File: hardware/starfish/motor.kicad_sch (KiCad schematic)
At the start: 24 parts, among them J7 MOTOR, U8 TMC2209

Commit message: First pass at schematic for starfish
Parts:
- added C1411: 100u, Capacitor_SMD:CP_Elec_6.3x9.9, symbol Device:C_Polarized_Small_US
- R1402: renamed from R18; value 220m -> 120m
- R1403: renamed from R19; value 220m -> 120m
- renumbered C28 to C1401, C29 to C1402, C30 to C1403, C31 to C1404, C32 to C1405, C33 to C1406, C38 to C1407, C39 to C1408, C40 to C1409, C41 to C1410, C35 to C1412, C36 to C1413, C37 to C1414, FB2 to FB1401, FB3 to FB1402, FB4 to FB1403, FB5 to FB1404, J7 to J1401, R17 to R1401, RV2 to RV1401, RV3 to RV1402, U8 to U1401
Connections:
- net GND: now also C1411.2
- net VS renamed +24V
- net +24V: now also C1411.1
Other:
- note added: "* Keep close to TMC2209 pin 28 (VS)"
- note added: "* Keep close to header"
- note added: "* Maximum current limited to 1.64 A(RMS) with R(sense) R18, R19 at 220mΩ * ESD & EME circuitry per Datasheet 3.7 * Bypass capacitors per Datasheet 3.1 * Internal clock set by CLK pulled low * SPREAD left floating since configuration is done via UART"
- note removed: "* Maximum current limited to 1 A(RMS) with R(sense) R18, R19 at 220mΩ * ESD & EME circuitry per Datasheet 3.7 * Bypass capacitors per Datasheet 3.1 * Internal clock set by CLK pulled low * SPREAD left floating since configuration is done via UART"
- title: Jellyfish -> Starfish
- moved on the sheet: C1401, C1402, C1403, C1404, C1405, C1406, C1407, C1408, C1409, C1410, C1412, C1413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

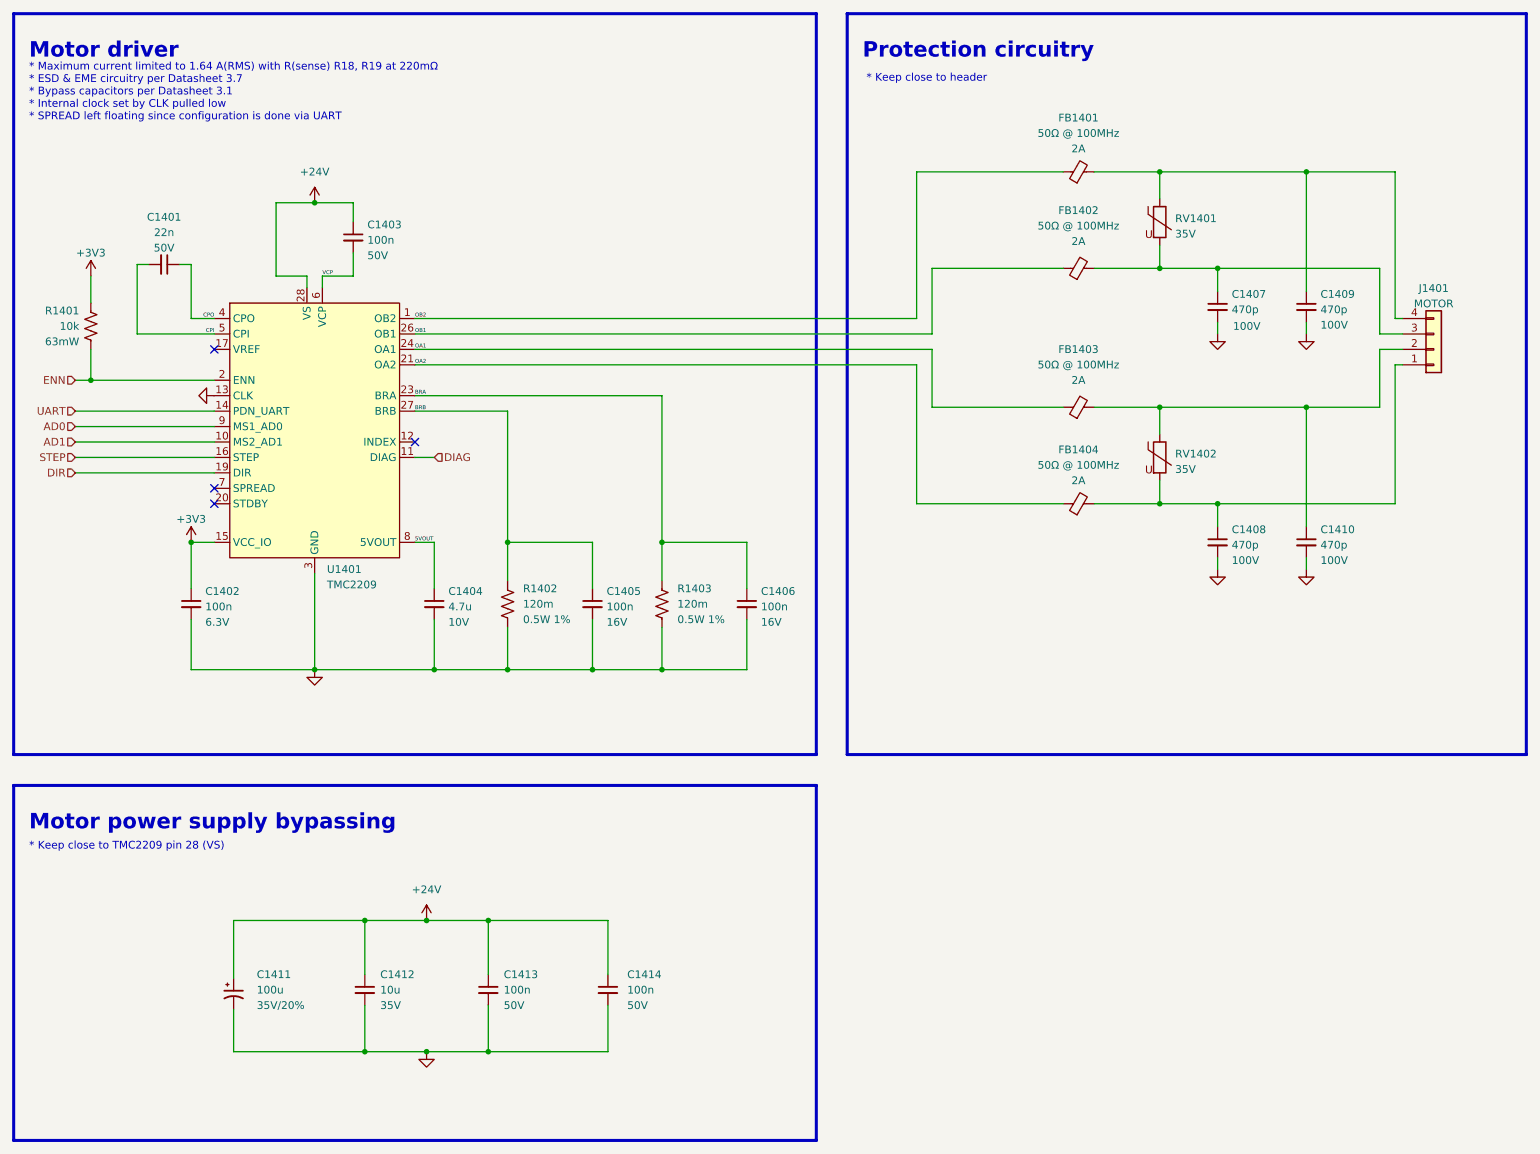
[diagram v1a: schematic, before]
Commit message: Mostly finished starfish schematic, ready for layout!
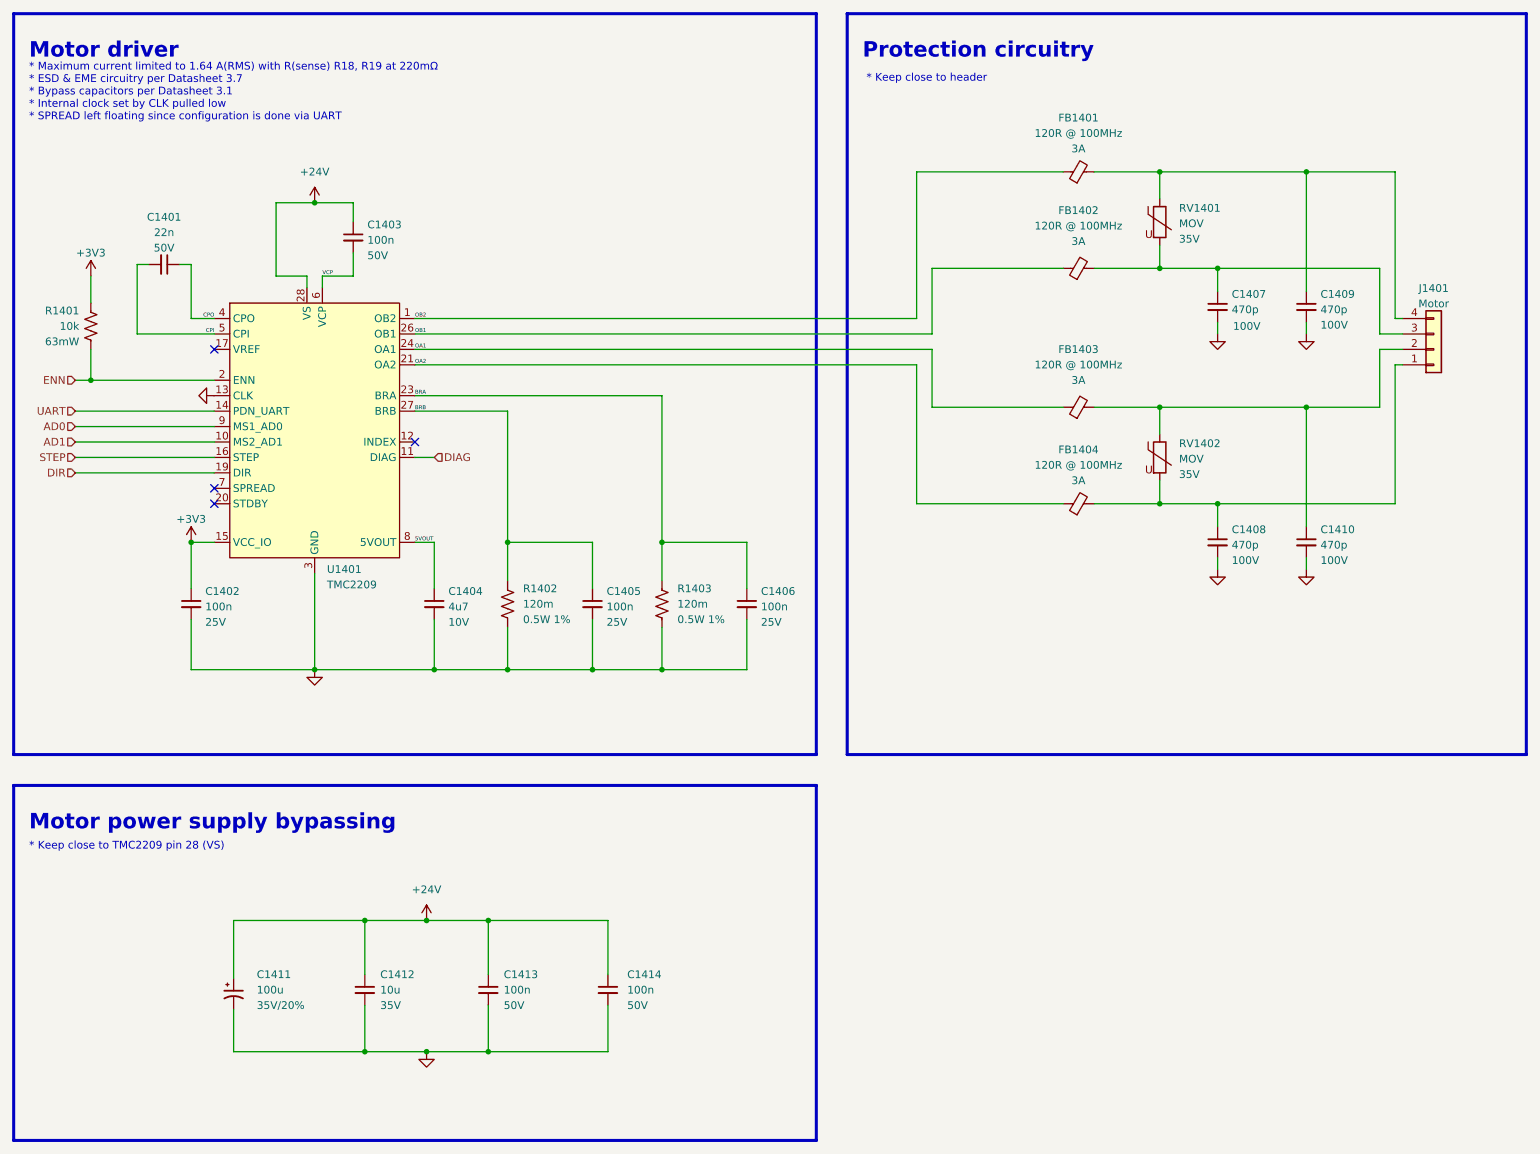
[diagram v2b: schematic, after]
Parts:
- C1401, C1403, C1407, C1408, C1409, C1410, C1413, C1414: footprint Capacitor_SMD:C_0603_1608Metric_Pad1.08x0.95mm_HandSolder -> winterbloom:C_0603_HandSolder
- C1402: footprint Capacitor_SMD:C_0402_1005Metric_Pad0.74x0.62mm_HandSolder -> winterbloom:C_0402_HandSolder; Rating 6.3V -> 25V
- C1404: value 4.7u -> 4u7; footprint Capacitor_SMD:C_0603_1608Metric_Pad1.08x0.95mm_HandSolder -> winterbloom:C_0603_HandSolder
- C1405, C1406: footprint Capacitor_SMD:C_0402_1005Metric_Pad0.74x0.62mm_HandSolder -> winterbloom:C_0402_HandSolder; Rating 16V -> 25V
- C1412: footprint Capacitor_SMD:C_1210_3225Metric_Pad1.33x2.70mm_HandSolder -> winterbloom:C_1210_HandSolder
- FB1401, FB1402, FB1403, FB1404: value 50Ω @ 100MHz -> 120R @ 100MHz; Rating 2A -> 3A
- J1401: value MOTOR -> Motor
- R1401: footprint Resistor_SMD:R_0402_1005Metric_Pad0.72x0.64mm_HandSolder -> winterbloom:R_0402_HandSolder
- RV1401, RV1402: value 35V -> MOV; Rating (none) -> 35V

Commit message: Layout and routing mostly done! Just gotta make it prettier!
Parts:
- FB1401, FB1402, FB1403, FB1404: footprint Inductor_SMD:L_0603_1608Metric_Pad1.05x0.95mm_HandSolder -> winterbloom:L_0603_HandSolder
- J1401: footprint Connector_JST:JST_XH_B4B-XH-AM_1x04_P2.50mm_Vertical -> winterbloom:JST_XH_B4B-XH-AM_1x04_P2.50mm_Vertical
- R1402, R1403: footprint Resistor_SMD:R_1206_3216Metric_Pad1.30x1.75mm_HandSolder -> winterbloom:R_1206_HandSolder
- RV1401, RV1402: footprint Resistor_SMD:R_0603_1608Metric_Pad0.98x0.95mm_HandSolder -> winterbloom:R_0603_HandSolder
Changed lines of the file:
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@@
       (effects (font (size 1.27 1.27)) (justify right))
     )
-    (property "Footprint" "Resistor_SMD:R_1206_3216Metric_Pad1.30x1.75mm_HandSolder" (id 2) (at 120.904 112.141 90)
+    (property "Footprint" "winterbloom:R_1206_HandSolder" (id 2) (at 120.904 112.141 90)
       (effects (font (size 1.27 1.27)) hide)
     )
@@
       (effects (font (size 1.27 1.27)) (justify left))
     )
-    (property "Footprint" "Resistor_SMD:R_0603_1608Metric_Pad0.98x0.95mm_HandSolder" (id 2) (at 202.057 88.265 90)
+    (property "Footprint" "winterbloom:R_0603_HandSolder" (id 2) (at 202.057 88.265 90)
       (effects (font (size 1.27 1.27)) hide)
     )
@@
     (property "Reference" "FB1402" (id 0) (at 190.4619 47.625 90))
     (property "Value" "120R @ 100MHz" (id 1) (at 190.4619 50.165 90))
-    (property "Footprint" "Inductor_SMD:L_0603_1608Metric_Pad1.05x0.95mm_HandSolder" (id 2) (at 190.5 58.928 90)
+    (property "Footprint" "winterbloom:L_0603_HandSolder" (id 2) (at 190.5 58.928 90)
       (effects (font (size 1.27 1.27)) hide)
     )
@@
       (effects (font (size 1.27 1.27)) (justify right))
     )
-    (property "Footprint" "Resistor_SMD:R_1206_3216Metric_Pad1.30x1.75mm_HandSolder" (id 2) (at 95.504 112.141 90)
+    (property "Footprint" "winterbloom:R_1206_HandSolder" (id 2) (at 95.504 112.141 90)
       (effects (font (size 1.27 1.27)) hide)
     )
@@
     (property "Reference" "FB1404" (id 0) (at 190.4619 86.995 90))
     (property "Value" "120R @ 100MHz" (id 1) (at 190.4619 89.535 90))
-    (property "Footprint" "Inductor_SMD:L_0603_1608Metric_Pad1.05x0.95mm_HandSolder" (id 2) (at 190.5 97.663 90)
+    (property "Footprint" "winterbloom:L_0603_HandSolder" (id 2) (at 190.5 97.663 90)
       (effects (font (size 1.27 1.27)) hide)
     )
@@
     (property "Reference" "FB1403" (id 0) (at 190.4619 70.485 90))
     (property "Value" "120R @ 100MHz" (id 1) (at 190.4619 73.025 90))
-    (property "Footprint" "Inductor_SMD:L_0603_1608Metric_Pad1.05x0.95mm_HandSolder" (id 2) (at 190.5 81.788 90)
+    (property "Footprint" "winterbloom:L_0603_HandSolder" (id 2) (at 190.5 81.788 90)
       (effects (font (size 1.27 1.27)) hide)
     )
@@
     (property "Reference" "J1401" (id 0) (at 248.92 60.4352 0))
     (property "Value" "Motor" (id 1) (at 248.92 62.9721 0))
-    (property "Footprint" "Connector_JST:JST_XH_B4B-XH-AM_1x04_P2.50mm_Vertical" (id 2) (at 248.92 70.485 0)
+    (property "Footprint" "winterbloom:JST_XH_B4B-XH-AM_1x04_P2.50mm_Vertical" (id 2) (at 248.92 70.485 0)
       (effects (font (size 1.27 1.27)) hide)
     )
@@
     (property "Reference" "FB1401" (id 0) (at 190.4619 32.385 90))
     (property "Value" "120R @ 100MHz" (id 1) (at 190.4619 34.925 90))
-    (property "Footprint" "Inductor_SMD:L_0603_1608Metric_Pad1.05x0.95mm_HandSolder" (id 2) (at 190.5 43.053 90)
+    (property "Footprint" "winterbloom:L_0603_HandSolder" (id 2) (at 190.5 43.053 90)
       (effects (font (size 1.27 1.27)) hide)
     )
@@
       (effects (font (size 1.27 1.27)) (justify left))
     )
-    (property "Footprint" "Resistor_SMD:R_0603_1608Metric_Pad0.98x0.95mm_HandSolder" (id 2) (at 202.057 49.53 90)
-      (effects (font (size 1.27 1.27)) hide)
-    )
+    (property "Footprint" "winterbloom:R_0603_HandSolder" (id 2) (at 202.057 49.53 90)
+      (effects (font (size 1.27 1.27)) hide)
+    )

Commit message: Run through purchasing, update some cap sizes
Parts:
- C1411: mpn (none) -> 865080653016, UWT1V221MNL1GS
- C1412: mpn CL32B106KBJNNNE -> CL32A106KAULNNE
- R1402, R1403: mpn KDV12DR240ET -> KDV12DR120ET
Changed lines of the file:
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@@
       (effects (font (size 1.27 1.27)) (justify left))
+    )
+    (property "mpn" "865080653016, UWT1V221MNL1GS" (id 5) (at 51.435 176.53 0)
+      (effects (font (size 1.27 1.27)) hide)
     )
     (pin "1")
@@
       (effects (font (size 1.27 1.27)) (justify right))
     )
-    (property "mpn" "KDV12DR240ET" (id 5) (at 121.92 112.395 0)
+    (property "mpn" "KDV12DR120ET" (id 5) (at 121.92 112.395 0)
       (effects (font (size 1.27 1.27)) hide)
     )
@@
       (effects (font (size 1.27 1.27)) (justify left))
     )
-    (property "mpn" "CL32B106KBJNNNE" (id 5) (at 73.025 175.895 0)
+    (property "mpn" "CL32A106KAULNNE" (id 5) (at 73.025 175.895 0)
       (effects (font (size 1.27 1.27)) hide)
     )
@@
       (effects (font (size 1.27 1.27)) (justify right))
     )
-    (property "mpn" "KDV12DR240ET" (id 5) (at 96.52 112.395 0)
-      (effects (font (size 1.27 1.27)) hide)
-    )
+    (property "mpn" "KDV12DR120ET" (id 5) (at 96.52 112.395 0)
+      (effects (font (size 1.27 1.27)) hide)
+    )
